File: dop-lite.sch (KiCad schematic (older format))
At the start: 23 parts, among them J1 Power Input, J2 Power Output, Q1 IRF7319, Q2 NMOS 40V×5A Vgsth<3, SW1 ON/OFF button, U1 IP2721_PHY, U2 LM2574N−12G_PHY

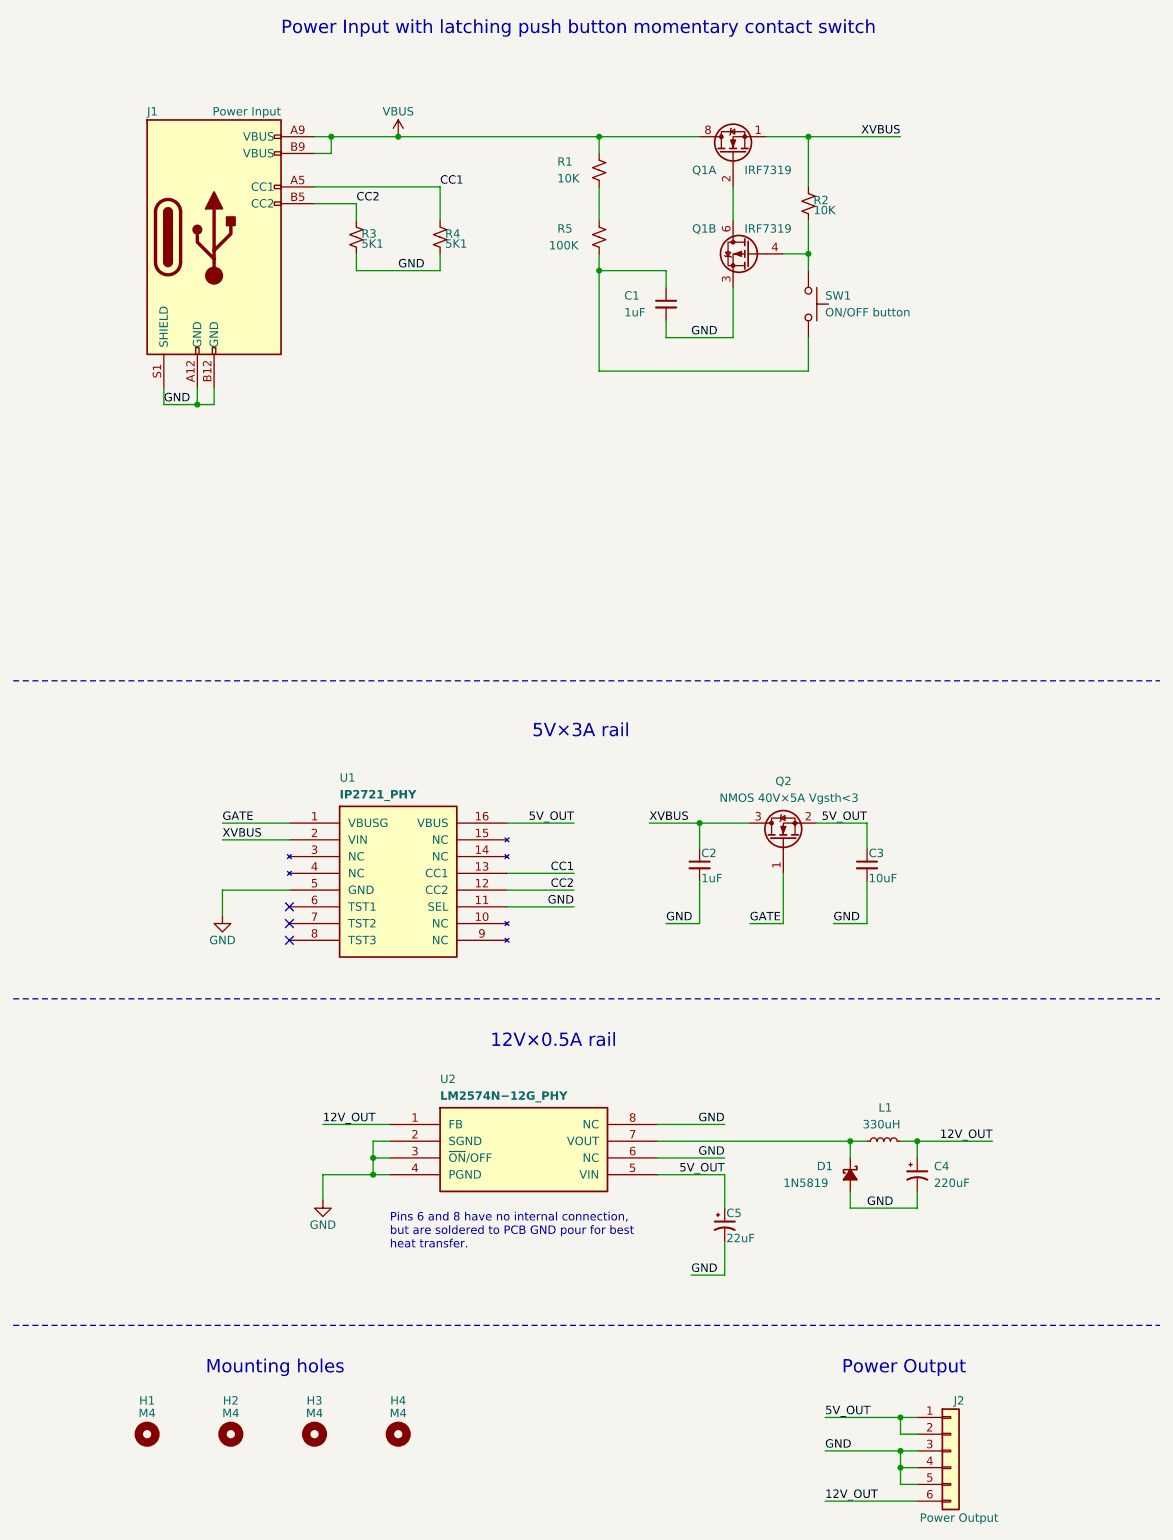
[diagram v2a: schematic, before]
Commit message: fixed power sources, no more ERC
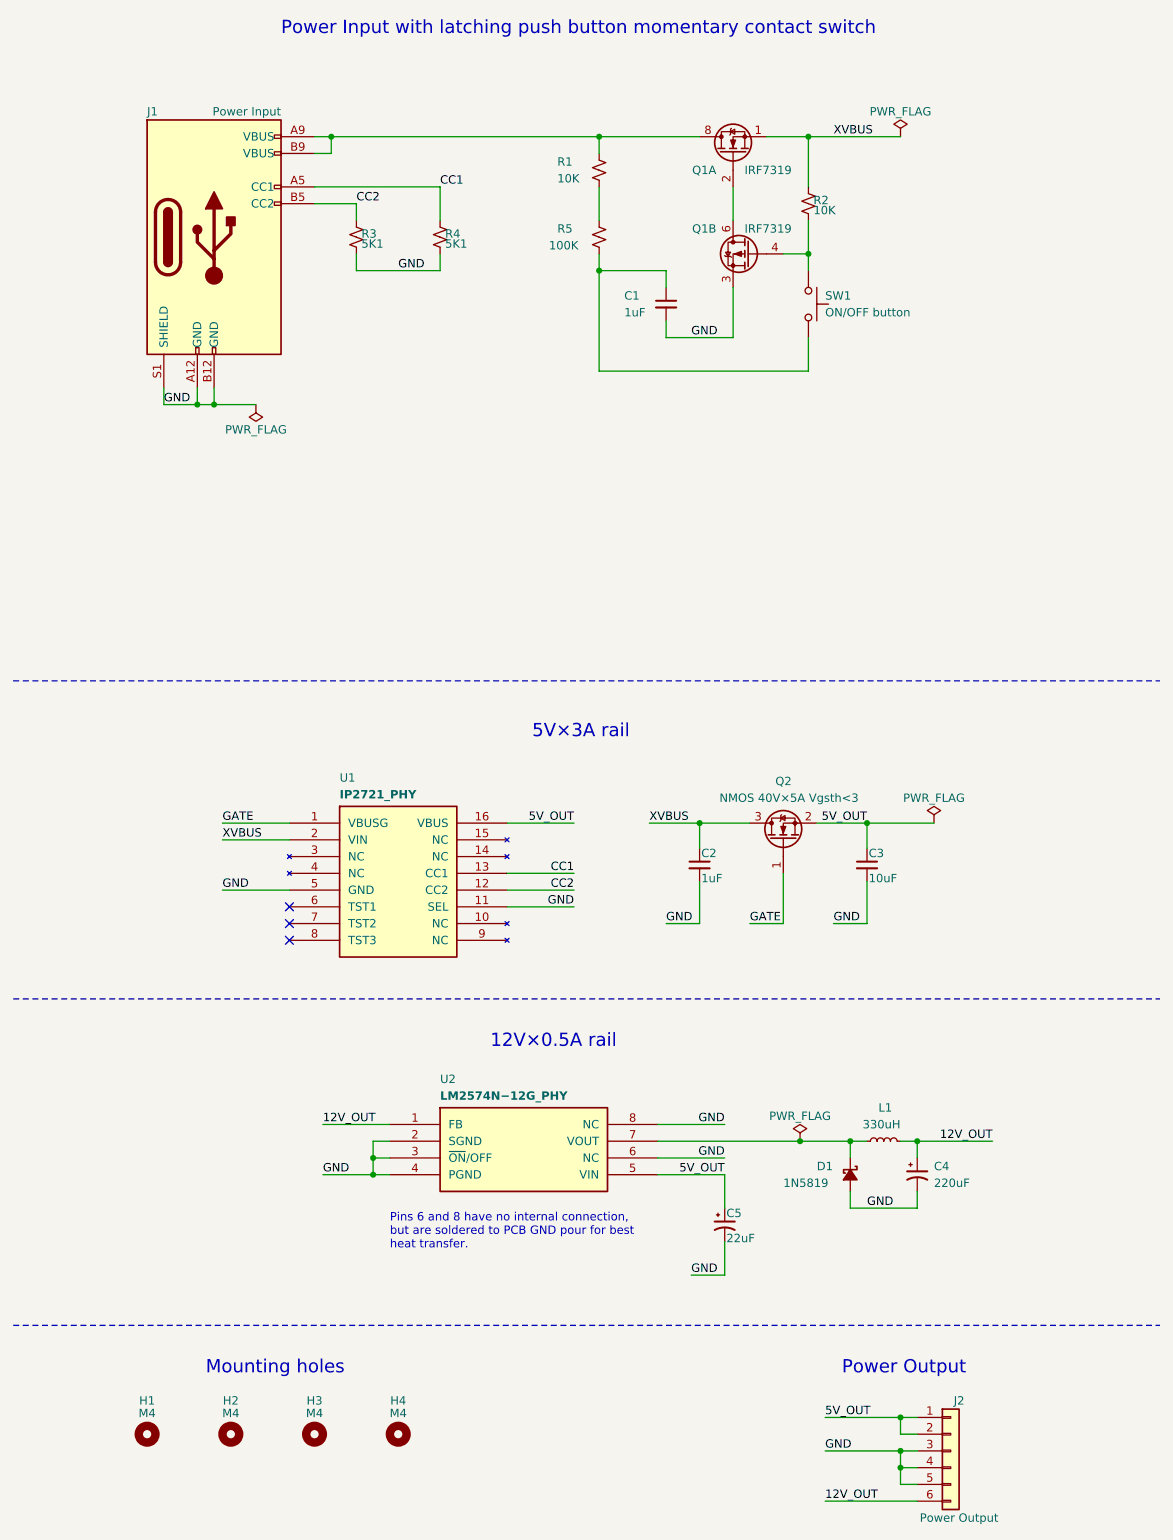
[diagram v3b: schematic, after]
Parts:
- H1, H2, H3, H4: footprint MountingHole:MountingHole_4.3mm_M4 -> MountingHole:MountingHole_4.3mm_M4_DIN965_Pad
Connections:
- net VBUS: no longer names the net of J1.A9 (VBUS), J1.B9 (VBUS), Q1.7 (D), Q1.8 (D), R1.1
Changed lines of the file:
@@
 Sheet 1 1
 Title "DOP `Delivery Of Power´ Lite"
-Date "2022-06-08"
+Date "2022-06-11"
 Rev "v1.0.0-draft"
 Comp "Sporniket-Studio.com"
-Comment1 ""
+Comment1 "Original source : https://github.com/sporniket/dop-lite"
 Comment2 ""
 Comment3 ""
@@
 	4550 7800 4950 7800
 Wire Wire Line
-	4550 7600 5700 7600
+	4550 7600 5400 7600
 Connection ~ 6100 7600
 Wire Wire Line
@@
 Text Notes 5650 9000 0    79   ~ 0
 Power Output
-$Comp
-L power:GND #PWR03
-U 1 1 62A8F091
-P 1950 6250
-F 0 "#PWR03" H 1950 6000 50  0001 C CNN
-F 1 "GND" H 1950 6100 50  0000 C CNN
-F 2 "" H 1950 6250 50  0001 C CNN
-F 3 "" H 1950 6250 50  0001 C CNN
-	1    1950 6250
-	1    0    0    -1
-$EndComp
-Wire Wire Line
-	1950 6250 1950 6100
 Text Label 5800 8000 0    50   ~ 0
 GND
@@
 Wire Wire Line
 	6100 8000 6100 7900
-$Comp
-L power:GND #PWR04
-U 1 1 62A96D55
-P 2550 7950
-F 0 "#PWR04" H 2550 7700 50  0001 C CNN
-F 1 "GND" H 2550 7800 50  0000 C CNN
-F 2 "" H 2550 7950 50  0001 C CNN
-F 3 "" H 2550 7950 50  0001 C CNN
-	1    2550 7950
-	1    0    0    -1
-$EndComp
-Wire Wire Line
-	2550 7950 2550 7800
 Wire Wire Line
 	2500 1600 2600 1600
@@
 	2600 1700 2600 1600
 Connection ~ 2600 1600
-Wire Wire Line
-	2600 1600 3000 1600
 Text Label 4950 7700 2    50   ~ 0
 GND
@@
 F 0 "H1" H 1500 9550 50  0000 C CNN
 F 1 "M4" H 1500 9475 50  0000 C CNN
-F 2 "MountingHole:MountingHole_4.3mm_M4" H 1500 9350 50  0001 C CNN
+F 2 "MountingHole:MountingHole_4.3mm_M4_DIN965_Pad" H 1500 9350 50  0001 C CNN
 F 3 "~" H 1500 9350 50  0001 C CNN
 	1    1500 9350
@@
 F 0 "H2" H 2000 9550 50  0000 C CNN
 F 1 "M4" H 2000 9475 50  0000 C CNN
-F 2 "MountingHole:MountingHole_4.3mm_M4" H 2000 9350 50  0001 C CNN
+F 2 "MountingHole:MountingHole_4.3mm_M4_DIN965_Pad" H 2000 9350 50  0001 C CNN
 F 3 "~" H 2000 9350 50  0001 C CNN
 	1    2000 9350
@@
 F 0 "H3" H 2500 9550 50  0000 C CNN
 F 1 "M4" H 2500 9475 50  0000 C CNN
-F 2 "MountingHole:MountingHole_4.3mm_M4" H 2500 9350 50  0001 C CNN
+F 2 "MountingHole:MountingHole_4.3mm_M4_DIN965_Pad" H 2500 9350 50  0001 C CNN
 F 3 "~" H 2500 9350 50  0001 C CNN
 	1    2500 9350
@@
 F 0 "H4" H 3000 9550 50  0000 C CNN
 F 1 "M4" H 3000 9475 50  0000 C CNN
-F 2 "MountingHole:MountingHole_4.3mm_M4" H 3000 9350 50  0001 C CNN
+F 2 "MountingHole:MountingHole_4.3mm_M4_DIN965_Pad" H 3000 9350 50  0001 C CNN
 F 3 "~" H 3000 9350 50  0001 C CNN
 	1    3000 9350
-	1    0    0    -1
-$EndComp
-$Comp
-L power:VBUS #PWR01
-U 1 1 62A987F5
-P 3000 1600
-F 0 "#PWR01" H 3000 1450 50  0001 C CNN
-F 1 "VBUS" H 3000 1750 50  0000 C CNN
-F 2 "" H 3000 1600 50  0001 C CNN
-F 3 "" H 3000 1600 50  0001 C CNN
-	1    3000 1600
 	1    0    0    -1
 $EndComp
@@
 Wire Wire Line
 	4200 2400 4200 2300
-Wire Wire Line
-	3000 1600 4200 1600
-Connection ~ 3000 1600
+Connection ~ 5450 1600
+Connection ~ 4200 1600
+Connection ~ 4200 2400
+Wire Wire Line
+	4200 1600 4800 1600
+Wire Wire Line
+	4500 5700 4800 5700
+$Comp
+L power:PWR_FLAG #FLG0101
+U 1 1 62A4CCCF
+P 6000 1600
+F 0 "#FLG0101" H 6000 1675 50  0001 C CNN
+F 1 "PWR_FLAG" H 6000 1750 50  0000 C CNN
+F 2 "" H 6000 1600 50  0001 C CNN
+F 3 "~" H 6000 1600 50  0001 C CNN
+	1    6000 1600
+	1    0    0    -1
+$EndComp
 Wire Wire Line
 	5450 1600 6000 1600
-Connection ~ 5450 1600
-Text Label 6000 1600 2    50   ~ 0
+Text Label 5600 1600 0    50   ~ 0
 XVBUS
 Text Label 1950 5800 0    50   ~ 0
@@
 Wire Wire Line
 	1950 5800 2350 5800
-Connection ~ 4200 1600
-Connection ~ 4200 2400
-Wire Wire Line
-	4200 1600 4800 1600
 Text Label 4500 5700 0    50   ~ 0
 XVBUS
 Wire Wire Line
-	4500 5700 4800 5700
+	1900 3200 2150 3200
+Connection ~ 1900 3200
+$Comp
+L power:PWR_FLAG #FLG0102
+U 1 1 62A5512F
+P 2150 3200
+F 0 "#FLG0102" H 2150 3275 50  0001 C CNN
+F 1 "PWR_FLAG" H 2150 3350 50  0000 C CNN
+F 2 "" H 2150 3200 50  0001 C CNN
+F 3 "~" H 2150 3200 50  0001 C CNN
+	1    2150 3200
+	-1   0    0    1
+$EndComp
+Wire Wire Line
+	5800 5700 6200 5700
+Connection ~ 5800 5700
+$Comp
+L power:PWR_FLAG #FLG0103
+U 1 1 62A5817E
+P 6200 5700
+F 0 "#FLG0103" H 6200 5775 50  0001 C CNN
+F 1 "PWR_FLAG" H 6200 5850 50  0000 C CNN
+F 2 "" H 6200 5700 50  0001 C CNN
+F 3 "~" H 6200 5700 50  0001 C CNN
+	1    6200 5700
+	1    0    0    -1
+$EndComp
+Text Label 2550 7800 0    50   ~ 0
+GND
+Text Label 1950 6100 0    50   ~ 0
+GND
+$Comp
+L power:PWR_FLAG #FLG0104
+U 1 1 62A586C6
+P 5400 7600
+F 0 "#FLG0104" H 5400 7675 50  0001 C CNN
+F 1 "PWR_FLAG" H 5400 7750 50  0000 C CNN
+F 2 "" H 5400 7600 50  0001 C CNN
+F 3 "~" H 5400 7600 50  0001 C CNN
+	1    5400 7600
+	1    0    0    -1
+$EndComp
+Connection ~ 5400 7600
+Wire Wire Line
+	5400 7600 5700 7600
+Wire Wire Line
+	2600 1600 4200 1600
 $EndSCHEMATC

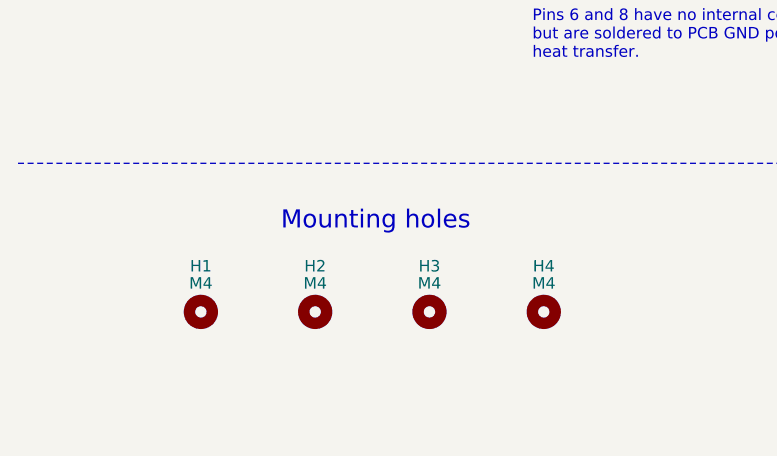
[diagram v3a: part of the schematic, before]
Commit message: Resolves #1 : Use M2.5 mounting hole
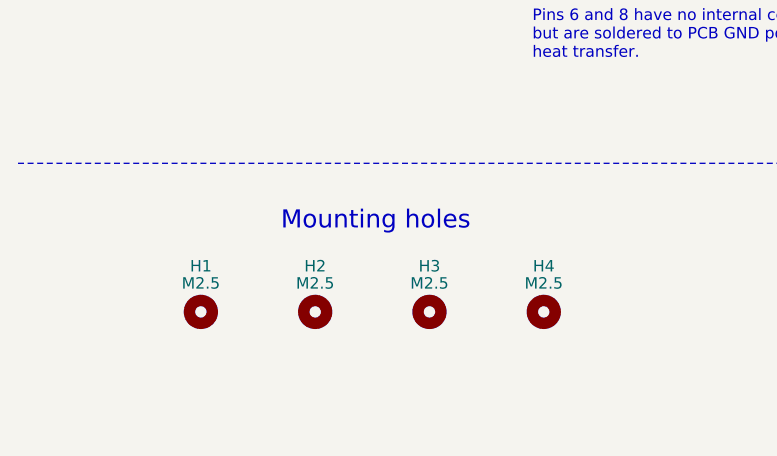
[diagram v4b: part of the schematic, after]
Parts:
- H1, H2, H3, H4: value M4 -> M2.5; footprint MountingHole:MountingHole_4.3mm_M4_DIN965_Pad -> MountingHole:MountingHole_2.7mm_M2.5_Pad
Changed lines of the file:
@@
 P 1500 9350
 F 0 "H1" H 1500 9550 50  0000 C CNN
-F 1 "M4" H 1500 9475 50  0000 C CNN
-F 2 "MountingHole:MountingHole_4.3mm_M4_DIN965_Pad" H 1500 9350 50  0001 C CNN
+F 1 "M2.5" H 1500 9475 50  0000 C CNN
+F 2 "MountingHole:MountingHole_2.7mm_M2.5_Pad" H 1500 9350 50  0001 C CNN
 F 3 "~" H 1500 9350 50  0001 C CNN
 	1    1500 9350
@@
 P 2000 9350
 F 0 "H2" H 2000 9550 50  0000 C CNN
-F 1 "M4" H 2000 9475 50  0000 C CNN
-F 2 "MountingHole:MountingHole_4.3mm_M4_DIN965_Pad" H 2000 9350 50  0001 C CNN
+F 1 "M2.5" H 2000 9475 50  0000 C CNN
+F 2 "MountingHole:MountingHole_2.7mm_M2.5_Pad" H 2000 9350 50  0001 C CNN
 F 3 "~" H 2000 9350 50  0001 C CNN
 	1    2000 9350
@@
 P 2500 9350
 F 0 "H3" H 2500 9550 50  0000 C CNN
-F 1 "M4" H 2500 9475 50  0000 C CNN
-F 2 "MountingHole:MountingHole_4.3mm_M4_DIN965_Pad" H 2500 9350 50  0001 C CNN
+F 1 "M2.5" H 2500 9475 50  0000 C CNN
+F 2 "MountingHole:MountingHole_2.7mm_M2.5_Pad" H 2500 9350 50  0001 C CNN
 F 3 "~" H 2500 9350 50  0001 C CNN
 	1    2500 9350
@@
 P 3000 9350
 F 0 "H4" H 3000 9550 50  0000 C CNN
-F 1 "M4" H 3000 9475 50  0000 C CNN
-F 2 "MountingHole:MountingHole_4.3mm_M4_DIN965_Pad" H 3000 9350 50  0001 C CNN
+F 1 "M2.5" H 3000 9475 50  0000 C CNN
+F 2 "MountingHole:MountingHole_2.7mm_M2.5_Pad" H 3000 9350 50  0001 C CNN
 F 3 "~" H 3000 9350 50  0001 C CNN
 	1    3000 9350
